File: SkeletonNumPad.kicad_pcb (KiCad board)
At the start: 2 copper layers, 76.2 x 95.2 mm, 68 parts, among them J1 USB_C_Receptacle_USB2.0, SW1 SW_PUSH, SW10 SW_PUSH, SW11 SW_PUSH, SW12 SW_PUSH, SW13 SW_PUSH, SW14 SW_PUSH, SW15 SW_PUSH, SW16 SW_PUSH, SW2 SW_PUSH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

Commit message: Customize footprints
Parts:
- added D17: D_Small, Diode_SMD:D_SOD-123, B.Cu at (150.7, 123.0)
- added LED17: YS-SK6812MINI-E, keyboard:YS-SK6812MINI-E, B.Cu at (114.4, 128.1)
- added SW17: SW_PUSH, Custom:MXOnly-1U-Hotswap, B.Cu at (142.9, 123.8)
- C1, C2, C3, C4, C5, C6, C7, C8, F1, PRTR5V0U2X1, R2, SW_RESET1, U1, Y1: moved to F.Cu
- R1: value 10k -> 5.1k; moved to F.Cu
- R3: value 5.1k -> 22; moved to F.Cu
- R4, R6: value 22 -> 10k; moved to F.Cu
- R5: value 10k -> 22; moved to F.Cu
- SW1, SW10, SW11, SW12, SW13, SW2, SW3, SW4, SW5, SW6, SW9: footprint MX_Only:MXOnly-1U-NoLED -> Custom:MXOnly-1U-Hotswap; moved to B.Cu
- SW14, SW7: footprint MX_Only:MXOnly-2U-VerticalStabilizers-NoLED -> Custom:MXOnly-1U-Hotswap; moved to B.Cu
- SW15: footprint MX_Only:MXOnly-2U-NoLED -> Custom:MXOnly-2U-Hotswap-VerticalStabilizers; moved to B.Cu
- SW16: footprint MX_Only:MXOnly-1U-NoLED -> Custom:MXOnly-2U-Hotswap; moved to B.Cu
- SW8: footprint MX_Only:MXOnly-1U-NoLED -> Custom:MXOnly-2U-Hotswap-VerticalStabilizers; moved to B.Cu
- moved R5 160.6 mm to (138.5, -87.5), turned to 0 degrees
- moved R1 159.3 mm to (130.0, -80.8)
- moved C8 152.9 mm to (155.1, -103.0), turned to 0 degrees
- moved C6 150.6 mm to (149.3, -99.7), turned to 0 degrees
- moved R3 136.3 mm to (133.3, -68.5), turned to 0 degrees
- moved R2 129.7 mm to (123.8, -65.5), turned to 0 degrees
- moved SW8 124.2 mm to (161.9, 76.2), turned to 180 degrees
- moved D8 124.1 mm to (169.8, 75.4)
- moved SW4 123.8 mm to (161.9, 47.6), turned to 180 degrees
- moved D4 123.8 mm to (169.8, 46.9)
- moved C5 115.3 mm to (118.5, -71.5), turned to 0 degrees
- moved SW15 114.7 mm to (161.9, 114.3), turned to 180 degrees
- moved D15 114.6 mm to (169.8, 113.5)
- moved C7 114.4 mm to (123.0, -71.5), turned to 0 degrees
- moved C2 112.0 mm to (124.3, -74.8), turned to 0 degrees
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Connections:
- D11 pad 1: row3 -> row2
- D15 pad 1: row4 -> row3
- D4 pad 1: row1 -> row0
- D8 pad 1: row2 -> row1
- LED16 pad 2: unconnected-(LED16-Pad2) -> Net-(LED16-Pad2)
- R1 pad 1: reset -> Net-(J1-PadA5)
- R1 pad 2: +5V -> GND
- R2 pad 1: Net-(J1-PadA5) -> Net-(J1-PadB5)
- R3 pad 1: Net-(J1-PadB5) -> Net-(J1-PadA7)
- R3 pad 2: GND -> d-
- R4 pad 1: Net-(J1-PadA7) -> Net-(R4-Pad1)
- R4 pad 2: d- -> GND
- R5 pad 1: Net-(R5-Pad1) -> Net-(J1-PadA6)
- R5 pad 2: GND -> d+
- R6 pad 1: Net-(J1-PadA6) -> reset
- R6 pad 2: d+ -> +5V
- SW1 pad 1: col1 -> col0
- SW10 pad 1: col2 -> col1
- SW11 pad 1: col0 -> col2
- SW12 pad 1: col1 -> col0
- SW13 pad 1: col2 -> col1
- SW14 pad 1: col3 -> col2
- SW15 pad 1: col0 -> col3
- SW16 pad 1: col2 -> col0
- SW2 pad 1: col2 -> col1
- SW3 pad 1: col3 -> col2
- SW4 pad 1: col0 -> col3
- SW5 pad 1: col1 -> col0
- SW6 pad 1: col2 -> col1
- SW7 pad 1: col3 -> col2
- SW8 pad 1: col0 -> col3
- SW9 pad 1: col1 -> col0
- U1 pad 1: Net-(R5-Pad1) -> Net-(R4-Pad1)
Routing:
- net GND: track 503.4 -> 0.00 mm, vias 1 -> 0
- net +5V: track 402.2 -> 0.00 mm, vias 6 -> 0
- net col3: track 114.9 -> 0.00 mm
- net row3: track 109.3 -> 0.00 mm, vias 2 -> 0
- net col2: track 100.8 -> 0.00 mm
- net row4: track 99.1 -> 0.00 mm, vias 2 -> 0
- net reset: track 96.5 -> 0.00 mm, vias 2 -> 0
- net col0: track 73.8 -> 0.00 mm
- net row1: track 72.8 -> 0.00 mm
- net col1: track 67.9 -> 0.00 mm
- net row2: track 66.5 -> 0.00 mm, vias 2 -> 0
- net row0: track 60.7 -> 0.00 mm, vias 2 -> 0
- net Net-(LED10-Pad2): track 47.1 -> 0.00 mm, vias 2 -> 0
- net Net-(LED3-Pad2): track 41.7 -> 0.00 mm, vias 2 -> 0
- net xtal1: track 34.0 -> 0.00 mm, vias 2 -> 0
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- removed copper zone on B.Cu, net GND
- removed copper zone on F.Cu, net GND
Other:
- board size 76.2 x 95.2 mm -> 76.2 x 104.8 mm

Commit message: with WS2812B-2020
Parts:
- removed PRTR5V0U2X1: PRTR5V0U2X, Package_TO_SOT_SMD:SOT-143
- removed SW_RESET1: SW_PUSH, Button_Switch_SMD:SW_SPST_SKQG_WithStem
- added SW_1: SW_PUSH, Button_Switch_SMD:SW_SPST_SKQG_WithStem, B.Cu at (128.6, 124.8)
- added U2: PRTR5V0U2X, Package_TO_SOT_SMD:SOT-143, B.Cu at (136.0, 53.0)
- C1, C2, C3, C4, C5, C6, C7, C8, F1, R1, R2, R3, R6, U1, Y1: moved to B.Cu
- J1: footprint Connector_USB:USB_C_Receptacle_HRO_TYPE-C-31-M-12 -> Connector_USB:USB_C_Receptacle_Palconn_UTC16-G
- LED1, LED10, LED11, LED12, LED13, LED14, LED15, LED16, LED17, LED2, LED3, LED4, LED5, LED6, LED7, LED8, LED9: value YS-SK6812MINI-E -> WS2812B; footprint keyboard:YS-SK6812MINI-E -> Custom:WS2812B-2020
- R4: value 10k -> 22; moved to B.Cu
- R5: value 22 -> 10k; moved to B.Cu
- moved C2 210.5 mm to (168.0, 131.1), turned to 90 degrees
- moved C1 204.4 mm to (160.3, 131.1), turned to -90 degrees
- moved R5 193.1 mm to (164.8, 103.8)
- moved Y1 186.0 mm to (164.0, 131.1), turned to 180 degrees
- moved C8 160.9 mm to (154.5, 57.9), turned to 90 degrees
- moved C3 160.9 mm to (170.5, 95.2), turned to 90 degrees
- moved R6 158.4 mm to (131.7, 119.0), turned to 90 degrees
- moved C6 157.9 mm to (160.2, 57.9), turned to 90 degrees
- moved C5 136.7 mm to (163.1, 57.9), turned to 90 degrees
- moved R3 134.8 mm to (161.6, 63.3), turned to -90 degrees
- moved C7 133.8 mm to (157.3, 57.9), turned to 90 degrees
- moved R4 124.8 mm to (164.4, 63.3), turned to -90 degrees
- moved C4 123.7 mm to (165.6, 57.9), turned to 90 degrees
- moved F1 122.2 mm to (114.3, 39.8), turned to -90 degrees
- moved R1 121.0 mm to (152.4, 38.1)
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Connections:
- R4 pad 1: Net-(R4-Pad1) -> Net-(J1-PadA6)
- R4 pad 2: GND -> d+
- R5 pad 1: Net-(J1-PadA6) -> Net-(R5-Pad1)
- R5 pad 2: d+ -> GND
- U1 pad 1: Net-(R4-Pad1) -> Net-(R5-Pad1)
- U1 pad 20: col3 -> unconnected-(U1-Pad20)
- U1 pad 21: col2 -> unconnected-(U1-Pad21)
- U1 pad 22: col1 -> unconnected-(U1-Pad22)
- U1 pad 26: row0 -> col0
- U1 pad 27: row1 -> col1
- U1 pad 28: row2 -> col2
- U1 pad 29: row3 -> col3
- U1 pad 30: row4 -> row0
- U1 pad 31: unconnected-(U1-Pad31) -> row1
- U1 pad 32: unconnected-(U1-Pad32) -> row2
- U1 pad 36: unconnected-(U1-Pad36) -> row3
- U1 pad 37: unconnected-(U1-Pad37) -> row4
- U1 pad 40: col0 -> unconnected-(U1-Pad40)
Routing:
- net GND: track 0.00 -> 492.6 mm, vias 0 -> 2
- net +5V: track 0.00 -> 450.9 mm, vias 0 -> 8
- net col0: track 0.00 -> 173.5 mm, vias 0 -> 7
- net col1: track 0.00 -> 132.8 mm, vias 0 -> 4
- net col2: track 0.00 -> 127.5 mm, vias 0 -> 5
- net col3: track 0.00 -> 121.2 mm
- net row0: track 0.00 -> 120.8 mm, vias 0 -> 2
- net row3: track 0.00 -> 88.6 mm, vias 0 -> 2
- net row1: track 0.00 -> 72.8 mm, vias 0 -> 2
- net row4: track 0.00 -> 71.8 mm, vias 0 -> 2
- net row2: track 0.00 -> 61.8 mm, vias 0 -> 2
- net Net-(J1-PadA6): track 0.00 -> 56.1 mm, vias 0 -> 2
- net xtal2: track 0.00 -> 53.6 mm, vias 0 -> 2
- net reset: track 0.00 -> 53.2 mm, vias 0 -> 2
- net Net-(J1-PadA7): track 0.00 -> 52.8 mm, vias 0 -> 2
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- added copper zone on B.Cu, net GND
- added copper zone on F.Cu, net GND
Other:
- board size 76.2 x 104.8 mm -> 80 x 104.8 mm

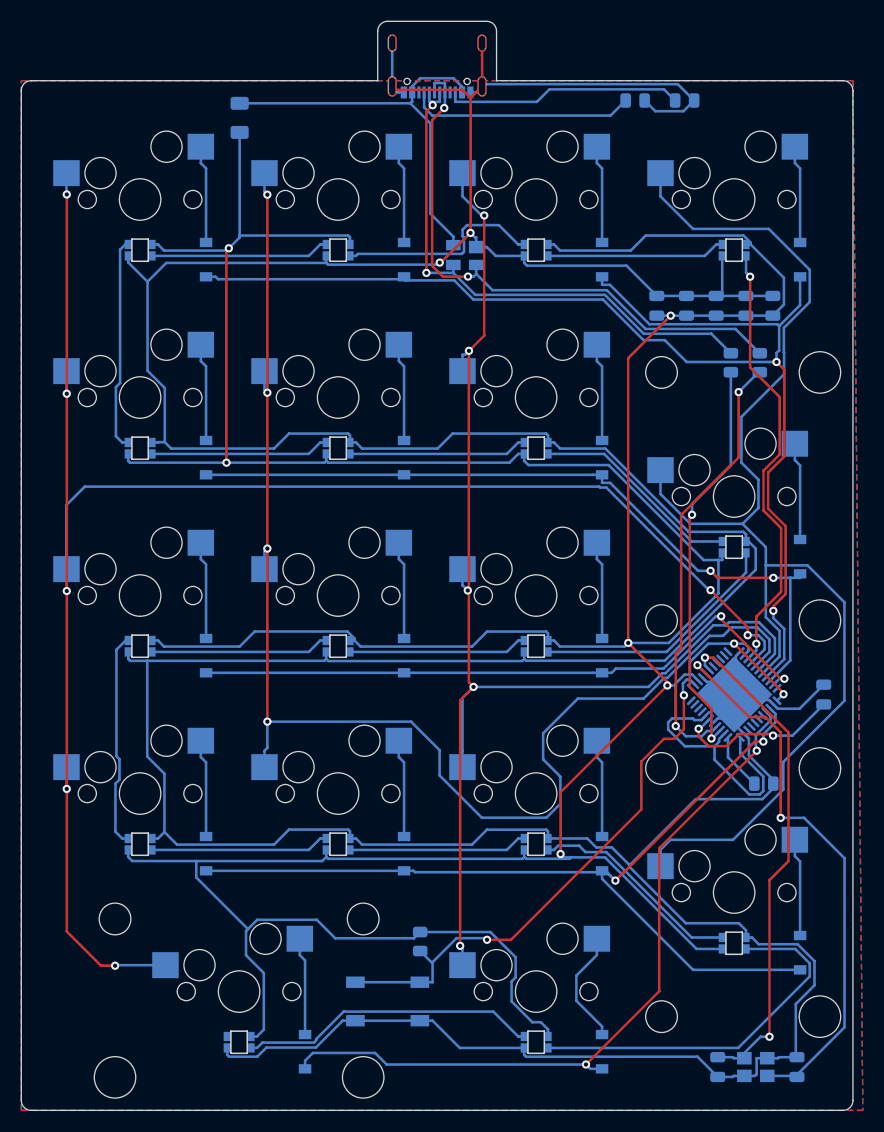
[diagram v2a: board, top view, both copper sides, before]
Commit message: with SK6812mini-e
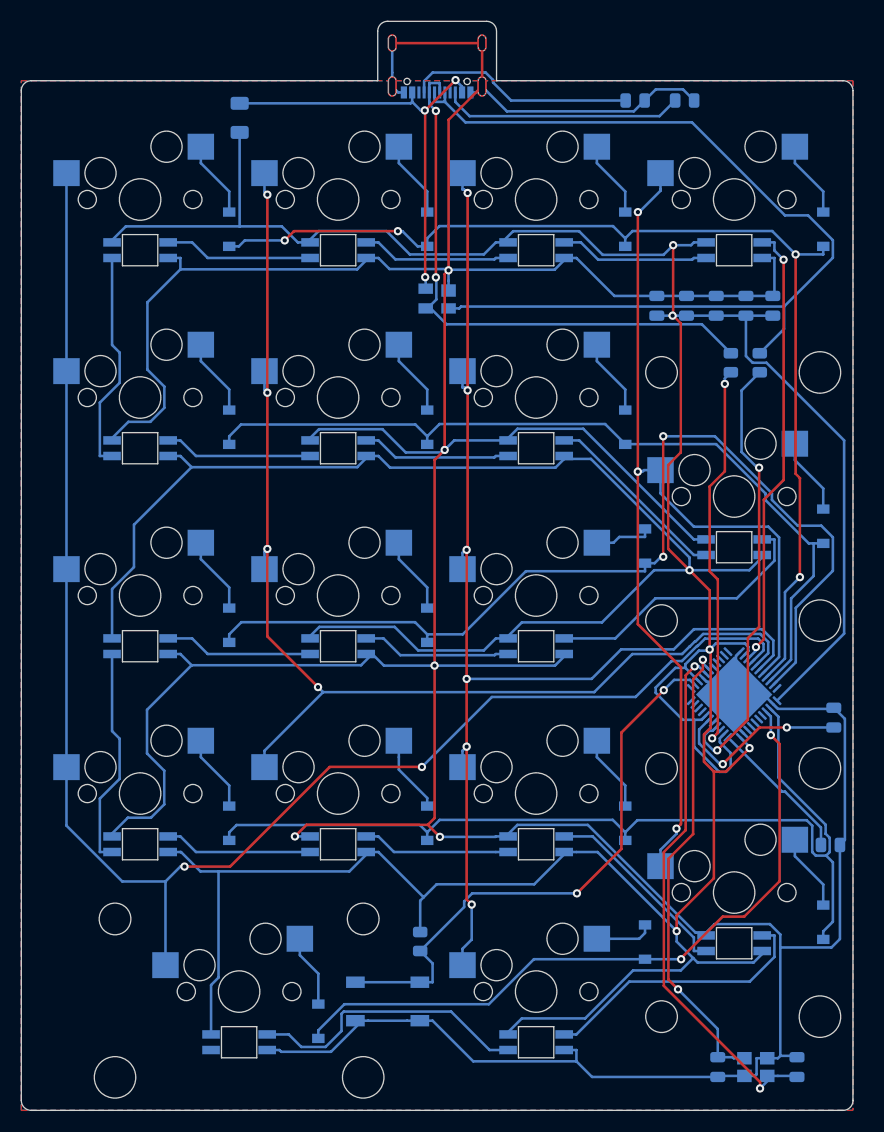
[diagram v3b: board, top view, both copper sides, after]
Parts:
- LED1, LED10, LED11, LED12, LED13, LED14, LED15, LED16, LED17, LED2, LED3, LED4, LED5, LED6, LED7, LED8, LED9: value WS2812B -> YS-SK6812MINI-E; footprint Custom:WS2812B-2020 -> Custom:YS-SK6812MINI-E
- moved D17 11.3 mm to (153.4, 119.1)
- moved D11 11.3 mm to (153.4, 81.0)
- moved R5 8.71 mm to (171.2, 109.7)
- moved U2 4.95 mm to (133.3, 57.1)
- moved D10 3.68 mm to (132.4, 88.6)
- moved D13 3.68 mm to (132.4, 107.6)
- moved D2 3.68 mm to (132.4, 50.5)
- moved D6 3.68 mm to (132.4, 69.5)
- moved D12 3.68 mm to (113.3, 107.6)
- moved D14 3.68 mm to (151.4, 107.6)
- moved D9 3.68 mm to (113.3, 88.6)
- moved D1 3.68 mm to (113.3, 50.5)
- moved D15 3.68 mm to (170.5, 117.2)
- moved D3 3.68 mm to (151.4, 50.5)
- moved D4 3.68 mm to (170.5, 50.5)
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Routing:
- net Net-(J1-PadA6): track 56.1 -> 91.8 mm, vias 2 -> 0
- net row2: track 61.8 -> 96.7 mm
- net col0: track 173.5 -> 152.3 mm, vias 7 -> 2
- net col3: track 121.2 -> 101.6 mm, vias 0 -> 3
- net +5V: track 450.9 -> 470.4 mm, vias 8 -> 6
- net col1: track 132.8 -> 114.4 mm
- net row0: track 120.8 -> 105.1 mm, vias 2 -> 4
- net Net-(LED15-Pad2): track 36.0 -> 26.6 mm
- net Net-(R5-Pad1): track 5.50 -> 14.2 mm
- net col2: track 127.5 -> 118.9 mm, vias 5 -> 6
- net row1: track 72.8 -> 80.3 mm, vias 2 -> 0
- net Net-(LED2-Pad2): track 20.2 -> 14.4 mm
- net Net-(D17-Pad2): track 11.1 -> 5.64 mm
- net row4: track 71.8 -> 68.0 mm
- net Net-(D11-Pad2): track 9.42 -> 5.64 mm
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
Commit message: rev1
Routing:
- net xtal1: track 45.4 -> 47.7 mm
- net xtal2: track 51.7 -> 53.9 mm
- net +5V: track 470.4 -> 471.5 mm
